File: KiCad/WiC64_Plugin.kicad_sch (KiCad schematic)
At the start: 55 parts, among them CN1 USERPORT-C64, Q1 BSS138, Q10 BSS138, Q11 BSS138, Q2 BSS138, Q3 BSS138, Q4 BSS138, Q5 BSS138, Q6 BSS138, Q7 BSS138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

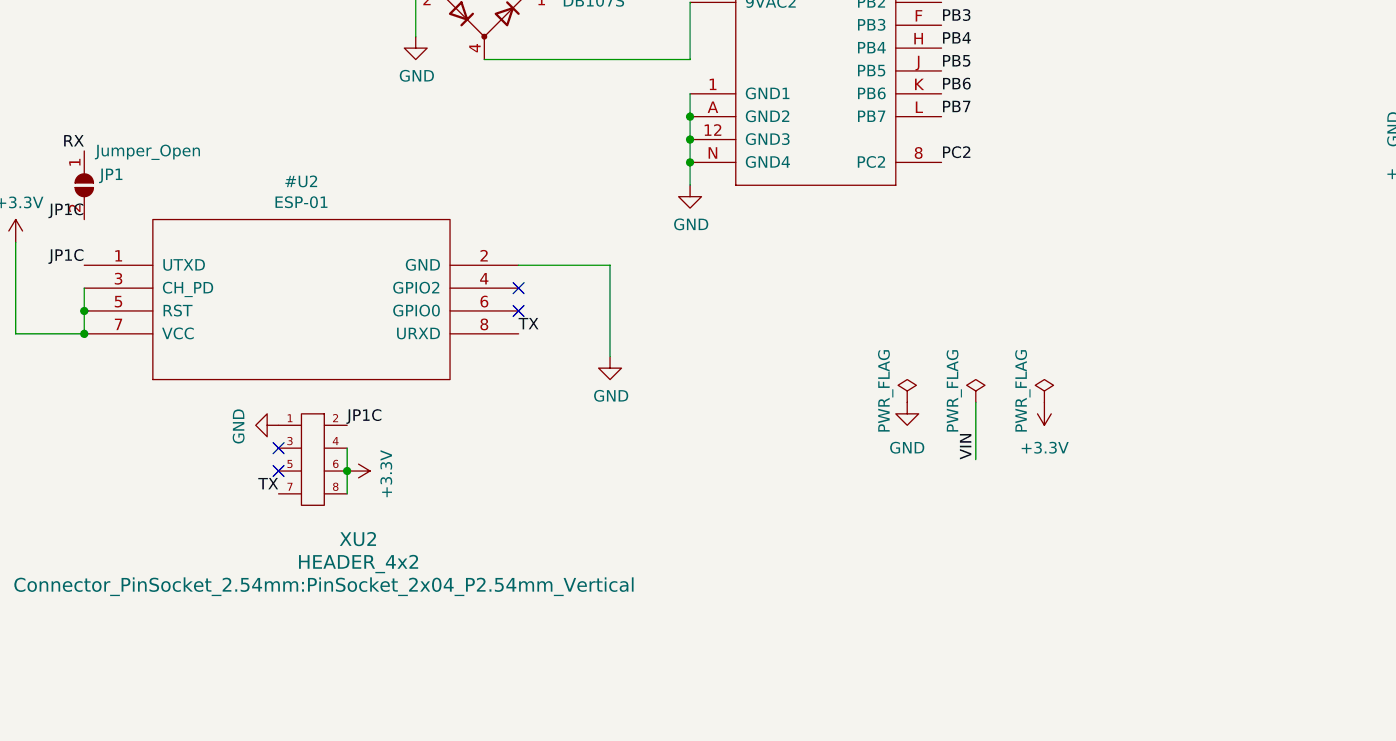
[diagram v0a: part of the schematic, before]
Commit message: Find/Reconstruct missing libs/footprints and fix most DRC problems PCB is mostly untouched so far, focus was just on "completing" the released source files
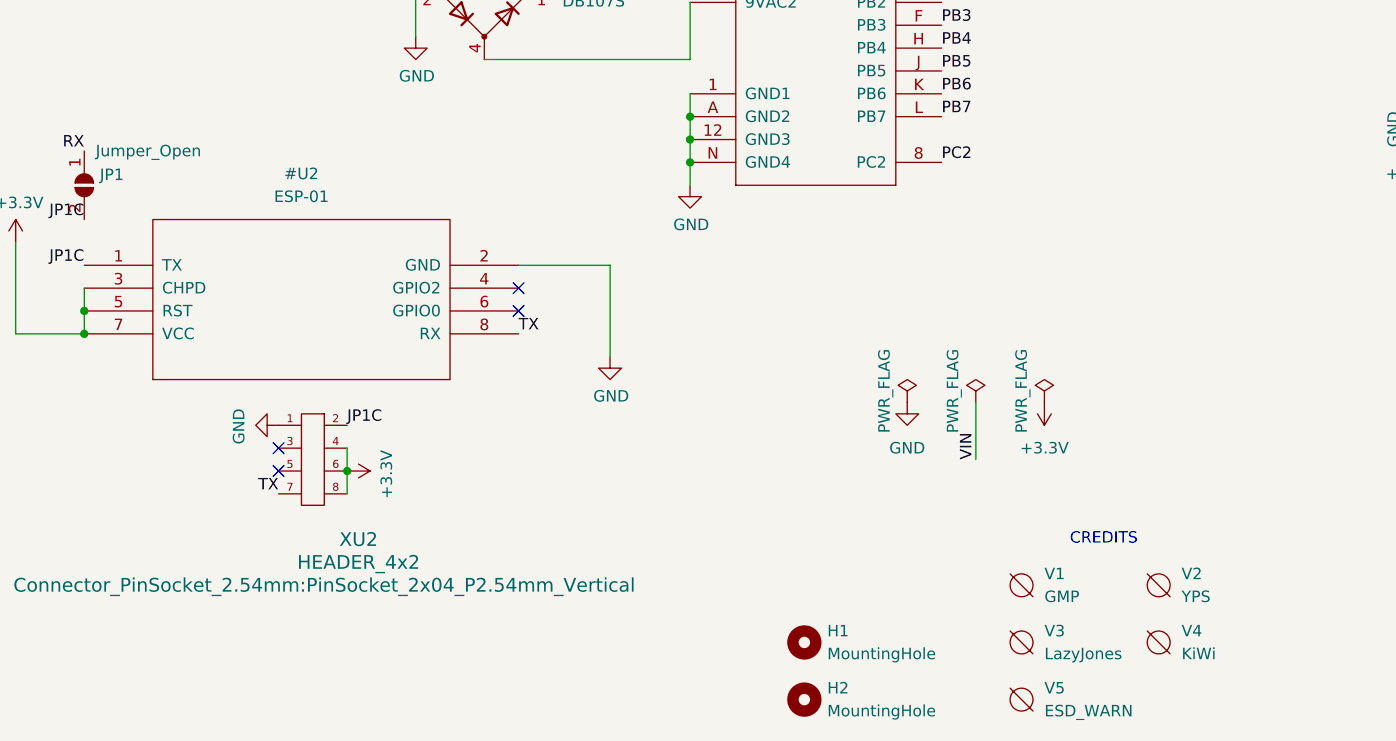
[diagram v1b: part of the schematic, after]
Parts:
- removed #U2: ESP-01, ESP8266:ESP-01, symbol ESP8266:ESP-01v090
- added #U2: ESP-01, ESP8266:ESP-01, symbol ESP8266:ESP-01
- added H1, H2: MountingHole, MountingHole:MountingHole_3.2mm_M3_ISO7380, symbol Mechanical:MountingHole
- added V1: GMP, Logo:GMP, symbol void:Void
- added V2: YPS, Logo:YPS2, symbol void:Void
- added V3: LazyJones, Logo:LazyJones2, symbol void:Void
- added V4: KiWi, Logo:KiWi, symbol void:Void
- added V5: ESD_WARN, Symbol:ESD-Logo_6.6x6mm_SilkScreen, symbol void:Void
- C1, C2: footprint w_capacitors:CP_6.3x11mm_hor -> w_capacitors:CP_6.3x11mm_horiz-R
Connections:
- net +3.3V: now also #U2.3 (CHPD), #U2.5 (RST), #U2.7 (VCC)
- net GND: now also #U2.2 (GND)
- net JP1C: now also #U2.1 (TX)
- net TX: now also #U2.8 (RX)
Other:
- note added: "CREDITS"
